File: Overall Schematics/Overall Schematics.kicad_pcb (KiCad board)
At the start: 2 copper layers, 1 part, among them U1 Teensy4.1

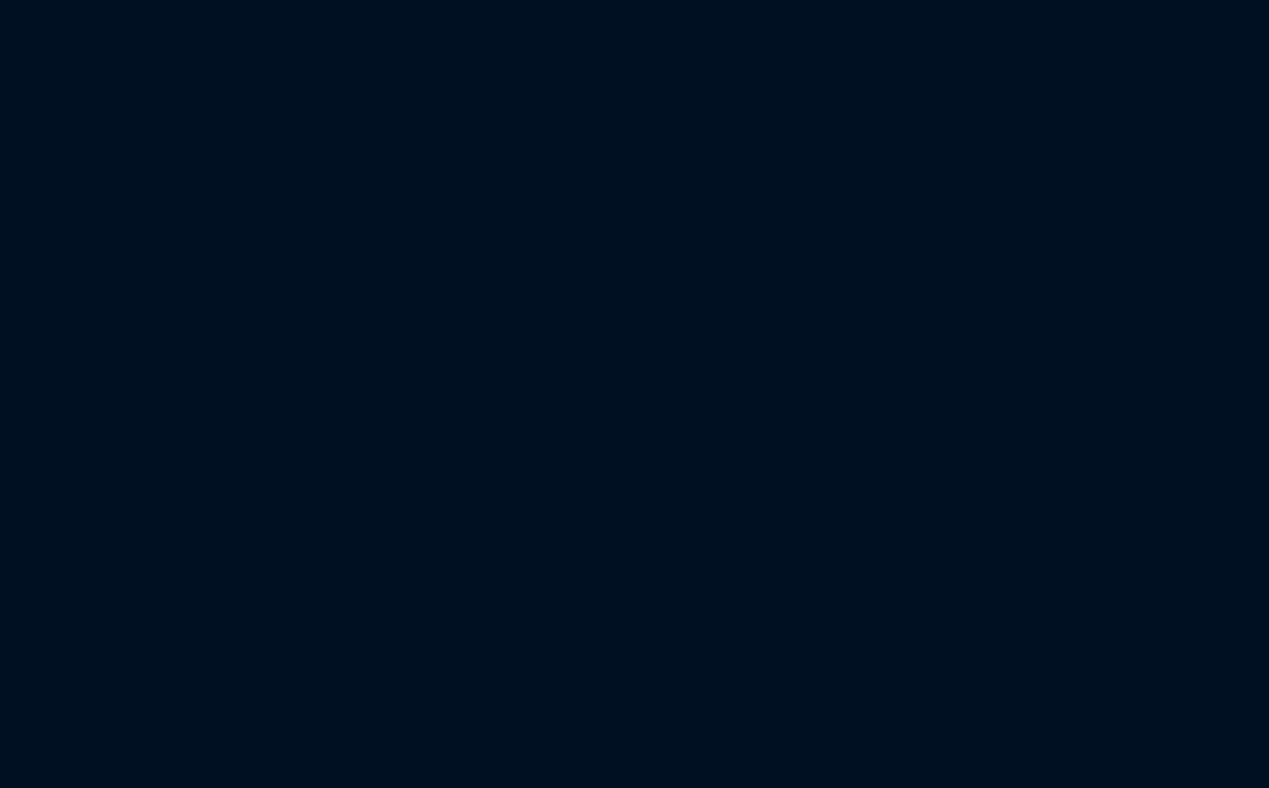
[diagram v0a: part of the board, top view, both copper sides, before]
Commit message: motor drive footprints completed (ready for pcb)
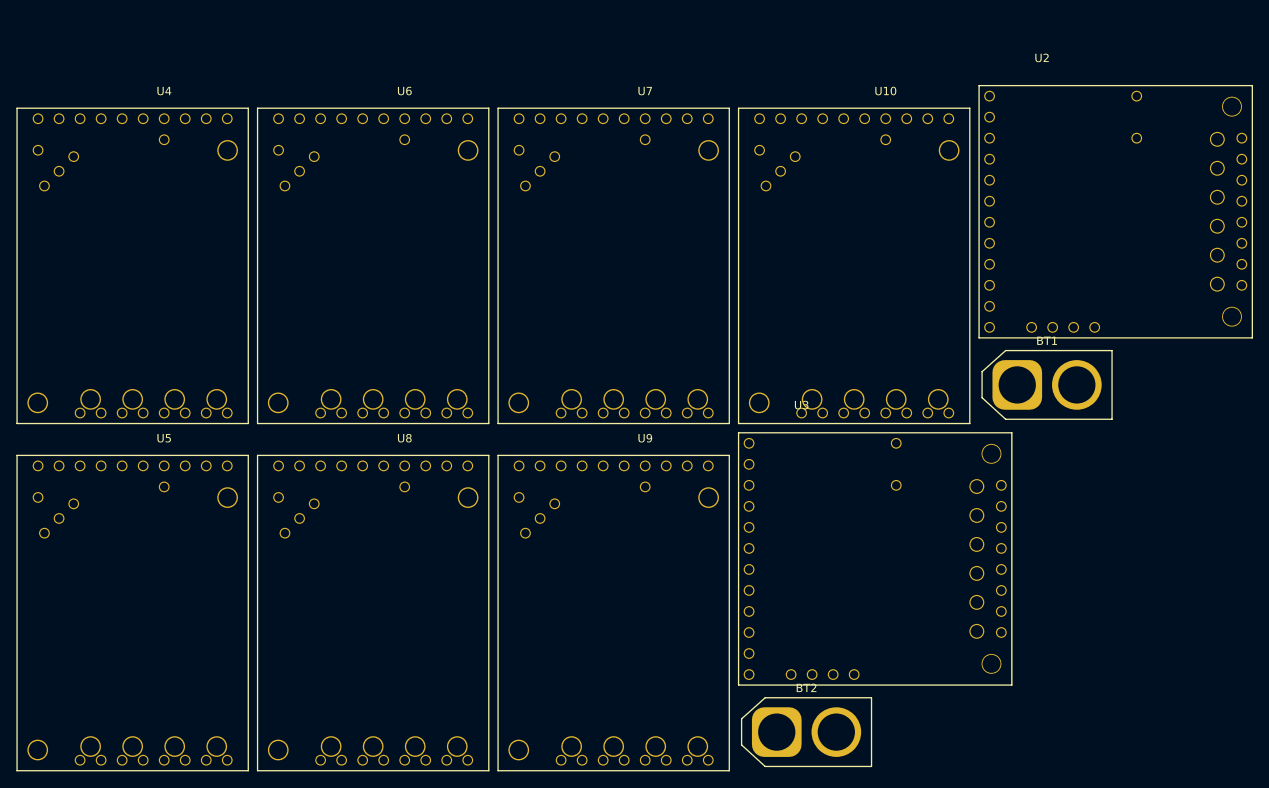
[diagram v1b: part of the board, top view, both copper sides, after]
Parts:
- added BT1: True_Spec_Battery1, Custom Footprints:AMASS_XT60-M_1x02_P7.20mm_Vertical, F.Cu at (267.0, 130.2)
- added BT2: True_Spec_Battery2, Custom Footprints:AMASS_XT60-M_1x02_P7.20mm_Vertical, F.Cu at (237.9, 172.2)
- added U10: VNH52019, Custom Footprints:DCMotorDriver, F.Cu at (251.1, 94.2)
- added U2: 36v4SMD, Custom Footprints:StepperMotorDriver, F.Cu at (270.0, 95.3)
- added U3: 36v4SMD, Custom Footprints:StepperMotorDriver, F.Cu at (240.9, 137.3)
- added U4: VNH52019, Custom Footprints:DCMotorDriver, F.Cu at (163.9, 94.2)
- added U5: VNH52019, Custom Footprints:DCMotorDriver, F.Cu at (163.9, 136.2)
- added U6: VNH52019, Custom Footprints:DCMotorDriver, F.Cu at (193.0, 94.2)
- added U7: VNH52019, Custom Footprints:DCMotorDriver, F.Cu at (222.0, 94.2)
- added U8: VNH52019, Custom Footprints:DCMotorDriver, F.Cu at (193.0, 136.2)
- added U9: VNH52019, Custom Footprints:DCMotorDriver, F.Cu at (222.0, 136.2)
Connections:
- net Net-(U1-Pad18) renamed LIN_SIGNAL1
- net Net-(U1-Pad19) renamed LIN_SIGNAL2
- net Net-(U1-Pad33) renamed LIN_SIGNAL3
- net Net-(U1-Pad49) renamed +24V
- U1 pad 1: Net-(U1-Pad1) -> GND
- U1 pad 11: Net-(U1-Pad11) -> INB_7
- U1 pad 12: Net-(U1-Pad12) -> INA_7
- U1 pad 13: Net-(U1-Pad13) -> PWM_7
- U1 pad 14: Net-(U1-Pad14) -> INA_2
- U1 pad 15: Net-(U1-Pad15) -> +3V3
- U1 pad 16: Net-(U1-Pad16) -> PWM_5
- U1 pad 17: Net-(U1-Pad17) -> PWM_6
- U1 pad 20: Net-(U1-Pad20) -> INA_5
- U1 pad 21: Net-(U1-Pad21) -> INB_5
- U1 pad 22: Net-(U1-Pad22) -> INA_6
- U1 pad 23: Net-(U1-Pad23) -> INB_6
- U1 pad 25: Net-(U1-Pad25) -> PWM_4
- U1 pad 26: Net-(U1-Pad26) -> INB_4
- U1 pad 27: Net-(U1-Pad27) -> INA_4
- U1 pad 28: Net-(U1-Pad28) -> INB_3
- U1 pad 29: Net-(U1-Pad29) -> PWM_3
- U1 pad 30: Net-(U1-Pad30) -> INA_3
- U1 pad 31: Net-(U1-Pad31) -> INB_2
- U1 pad 32: Net-(U1-Pad32) -> PWM_2
- U1 pad 34: Net-(U1-Pad34) -> GND
- U1 pad 35: Net-(U1-Pad35) -> INB_1
- U1 pad 36: Net-(U1-Pad36) -> PWM_1
- U1 pad 37: Net-(U1-Pad37) -> INA_1
- U1 pad 38: Net-(U1-Pad38) -> RESET_2
- U1 pad 39: Net-(U1-Pad39) -> SLEEP_2
- U1 pad 40: Net-(U1-Pad40) -> DIR_2
- U1 pad 41: Net-(U1-Pad41) -> STEP_2
- U1 pad 42: Net-(U1-Pad42) -> RESET_1
- U1 pad 43: Net-(U1-Pad43) -> SLEEP_1
- U1 pad 44: Net-(U1-Pad44) -> DIR_1
- U1 pad 45: Net-(U1-Pad45) -> STEP_1
- U1 pad 46: Net-(U1-Pad46) -> +3V3
- U1 pad 47: Net-(U1-Pad47) -> GND

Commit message: beginning of the pcb
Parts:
- added J1: WattMeter1_Output, TerminalBlock:TerminalBlock_bornier-2_P5.08mm, F.Cu at (246.4, 77.5)
- added J2: WattMeter2_Output, TerminalBlock:TerminalBlock_bornier-2_P5.08mm, F.Cu at (246.4, 104.1)
- added J3: Intel_Buck_Converter_Input, TerminalBlock:TerminalBlock_bornier-2_P5.08mm, F.Cu at (186.7, 114.3)
- added J4: WattMeter1_Input, TerminalBlock:TerminalBlock_bornier-2_P5.08mm, F.Cu at (246.4, 90.2)
- added J5: WattMeter2_Input, TerminalBlock:TerminalBlock_bornier-2_P5.08mm, F.Cu at (215.9, 113.0)
- added M1: Stepper_Motor_bipolar, TerminalBlock:TerminalBlock_bornier-4_P5.08mm, F.Cu at (104.1, 87.6)
- added M2: Stepper_Motor_bipolar, TerminalBlock:TerminalBlock_bornier-4_P5.08mm, F.Cu at (104.1, 120.7)
- added M3: LinActuator12V, TerminalBlock:TerminalBlock_bornier-5_P5.08mm, F.Cu at (-58.4, 158.8)
- added M4: LinActuator12V, TerminalBlock:TerminalBlock_bornier-5_P5.08mm, F.Cu at (-57.1, 101.6)
- added M5: LinActuator12V, TerminalBlock:TerminalBlock_bornier-5_P5.08mm, F.Cu at (-58.4, 128.3)
- added M6: Motor_DC, TerminalBlock:TerminalBlock_bornier-2_P5.08mm, F.Cu at (108.0, 215.9)
- added M7: Motor_DC, TerminalBlock:TerminalBlock_bornier-2_P5.08mm, F.Cu at (110.5, 240.0)
- added M8: Motor_DC, TerminalBlock:TerminalBlock_bornier-2_P5.08mm, F.Cu at (114.3, 158.8)
- added M9: Motor_DC, TerminalBlock:TerminalBlock_bornier-2_P5.08mm, F.Cu at (108.0, 188.0)
- added SW1: SW_DPST, Button_Switch_SMD:SW_MEC_5GSH9, F.Cu at (213.4, 85.1)
- BT1, BT2: footprint Custom Footprints:AMASS_XT60-M_1x02_P7.20mm_Vertical -> Custom Footprints:AMASS_XT60-F_1x02_P7.20mm_Vertical
- moved U10 245.9 mm to (52.1, 238.8), turned to 90 degrees
- moved U2 208.0 mm to (62.2, 85.1)
- moved U9 185.6 mm to (52.1, 210.8), turned to 90 degrees
- moved U6 182.0 mm to (15.2, 133.3), turned to 270 degrees
- moved U7 181.7 mm to (50.8, 154.9), turned to 90 degrees
- moved U3 180.0 mm to (62.2, 115.6)
- moved U1 165.6 mm to (38.1, 115.6), turned to 270 degrees
- moved U4 164.2 mm to (14.0, 161.3), turned to 270 degrees
- moved U5 152.9 mm to (15.2, 100.3), turned to 270 degrees
- moved U8 149.6 mm to (50.8, 182.9), turned to 90 degrees
- moved BT2 108.2 mm to (183.3, 78.7)
- moved BT1 92.1 mm to (182.9, 92.7)
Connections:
- U10 pad 11: OUTB_4 -> OUTA_4
- U10 pad 12: PWR_GND -> OUTB_4
- U10 pad 13: Battery1_Positive24V -> PWR_GND
- U10 pad 14: (no net) -> Battery1_Positive24V
- U4 pad 10: OUTA2_LIN -> Net-(U4-Pad10)
- U4 pad 11: OUTB2_LIN -> OUTA2_LIN
- U4 pad 12: PWR_GND -> OUTB2_LIN
- U4 pad 13: Battery1_Positive24V -> PWR_GND
- U4 pad 14: (no net) -> Battery1_Positive24V
- U5 pad 10: OUTA3_LIN -> Net-(U5-Pad10)
- U5 pad 11: OUTB3_LIN -> OUTA3_LIN
- U5 pad 12: PWR_GND -> OUTB3_LIN
- U5 pad 13: Battery1_Positive24V -> PWR_GND
- U5 pad 14: (no net) -> Battery1_Positive24V
- U6 pad 10: OUTA1_LIN -> Net-(U6-Pad10)
- U6 pad 11: OUTB1_LIN -> OUTA1_LIN
- U6 pad 12: PWR_GND -> OUTB1_LIN
- U6 pad 13: Battery1_Positive24V -> PWR_GND
- U6 pad 14: (no net) -> Battery1_Positive24V
- U7 pad 11: OUTB_1 -> OUTA_1
- U7 pad 12: PWR_GND -> OUTB_1
- U7 pad 13: Battery1_Positive24V -> PWR_GND
- U7 pad 14: (no net) -> Battery1_Positive24V
- U8 pad 11: OUTB_2 -> OUTA_2
- U8 pad 12: PWR_GND -> OUTB_2
- U8 pad 13: Battery1_Positive24V -> PWR_GND
- U8 pad 14: (no net) -> Battery1_Positive24V
- U9 pad 11: OUTB_3 -> OUTA_3
- U9 pad 12: PWR_GND -> OUTB_3
- U9 pad 13: Battery1_Positive24V -> PWR_GND
- U9 pad 14: (no net) -> Battery1_Positive24V

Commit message: started PCB traces, need to add maestro servo board stuff
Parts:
- moved M6 195.8 mm to (-63.0, 120.4), turned to 270 degrees
- moved U10 97.5 mm to (5.33, 153.2)
- moved U9 90.8 mm to (10.2, 130.3), turned to 270 degrees
- moved M7 86.9 mm to (70.1, 163.1), turned to 90 degrees
- moved M4 80.4 mm to (-61.5, 21.3), turned to 270 degrees
- moved U2 70.6 mm to (56.4, 14.7)
- moved M5 69.2 mm to (-62.7, 59.2), turned to 270 degrees
- moved U5 68.5 mm to (10.9, 32.0)
- moved U6 66.7 mm to (10.4, 66.8)
- moved M3 66.0 mm to (-63.2, 93.0), turned to 270 degrees
- moved U1 65.8 mm to (26.7, 50.8)
- moved U3 65.1 mm to (55.9, 50.8)
- moved U7 62.6 mm to (44.5, 92.7)
- moved U4 62.3 mm to (10.7, 99.1)
- moved M1 61.6 mm to (121.9, 28.7), turned to 270 degrees
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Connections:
- BT1 pad 2: Common_Ground -> PWR_GND
- BT2 pad 2: Common_Ground -> PWR_GND
- J1 pad 1: Common_Ground -> PWR_GND
- J2 pad 1: Common_Ground -> PWR_GND
- J3 pad 2: Common_Ground -> PWR_GND
- J4 pad 2: Common_Ground -> PWR_GND
- J5 pad 2: Common_Ground -> PWR_GND
- U1 pad 11: INB_7 -> Net-(U1-Pad11)
- U1 pad 12: INA_7 -> Net-(U1-Pad12)
- U1 pad 13: PWM_7 -> Net-(U1-Pad13)
- U1 pad 14: INA_2 -> INA_3
- U1 pad 30: INA_3 -> INA_2
- U1 pad 31: INB_2 -> PWM_2
- U1 pad 32: PWM_2 -> INB_2
- U1 pad 35: INB_1 -> INA_1
- U1 pad 37: INA_1 -> INB_1
- U1 pad 4: Net-(U1-Pad4) -> INA_7
- U1 pad 5: Net-(U1-Pad5) -> PWM_7
- U1 pad 6: Net-(U1-Pad6) -> INB_7
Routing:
- net INA_2: track 0.00 -> 78.7 mm
- net PWM_2: track 0.00 -> 74.7 mm
- net INB_2: track 0.00 -> 70.2 mm
- net INA_1: track 0.00 -> 59.1 mm
- net PWM_1: track 0.00 -> 56.6 mm
- net INB_1: track 0.00 -> 51.5 mm
- net RESET_2: track 0.00 -> 38.2 mm
- net SLEEP_2: track 0.00 -> 37.9 mm
- net DIR_2: track 0.00 -> 27.9 mm
- net STEP_2: track 0.00 -> 27.6 mm
- net INA_7: track 0.00 -> 18.4 mm
- net SLEEP_1: track 0.00 -> 17.9 mm
- net RESET_1: track 0.00 -> 17.9 mm
- net STEP_1: track 0.00 -> 16.8 mm
- net DIR_1: track 0.00 -> 16.8 mm
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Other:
- net class Power added: clearance 0.2, trace_width 0.5, via_dia 0.8, via_drill 0.4
- net class Signal added: clearance 0.2, trace_width 0.25, via_dia 0.8, via_drill 0.4

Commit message: fixed stuff
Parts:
- moved U2 2.84 mm to (55.9, 17.5)
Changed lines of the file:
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@@
   )
   (module "Custom Footprints:StepperMotorDriver" (layer F.Cu)
-    (at 56.388 14.732)
+    (at 55.88 17.526)
     (fp_text reference U2 (at 0 -4.58) (layer F.SilkS)
       (effects (font (size 1 1) (thickness 0.15)))

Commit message: new symbol
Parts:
- moved U6 5.93 mm to (11.4, 61.0)

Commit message: added 6 in cutout
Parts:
- moved BT1 572.3 mm to (668.5, 395.5)
- moved J1 572.3 mm to (732.0, 380.2)
- moved J2 572.3 mm to (732.0, 406.9)
- moved J4 572.3 mm to (732.0, 392.9)
- moved J5 572.3 mm to (701.5, 415.8)
- moved M4 572.3 mm to (424.2, 324.1)
- moved M5 572.3 mm to (422.9, 361.9)
- moved M6 572.3 mm to (422.7, 423.2)
- moved SW1 572.3 mm to (699.0, 387.9)
- moved U10 572.3 mm to (491.0, 455.9)
- moved U2 572.3 mm to (541.5, 320.3)
- moved U3 572.3 mm to (541.5, 353.6)
- moved BT2 572.3 mm to (668.9, 381.5)
- moved J3 572.3 mm to (672.3, 417.1)
- moved M1 572.3 mm to (607.6, 331.5)
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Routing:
- net INA_7: track 18.4 -> 0.00 mm
- net PWM_7: track 16.0 -> 0.00 mm
- net INB_7: track 13.9 -> 0.00 mm
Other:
- board outline added: 152.4 x 152.4 mm
